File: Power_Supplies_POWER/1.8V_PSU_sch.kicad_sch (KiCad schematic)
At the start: 35 parts, among them IC6 TLV71209DBVT, IC7 TPS73618DBVTG4, IC8 TLV73333PDBVR, IC9 TLV73333PDBVR, J1 PINHD_1x4_Female, J23 PINHD_1x2_Female, J24 PINHD_1x2_Female, J25 Screw_Terminal_4_P5.00mm, J26 PINHD_1x1_Female, J28 PINHD_1x5_Female, J29 PINHD_1x2_Female, J30 PINHD_1x2_Female, J31 PINHD_1x2_Female, J32 PINHD_1x1_Female

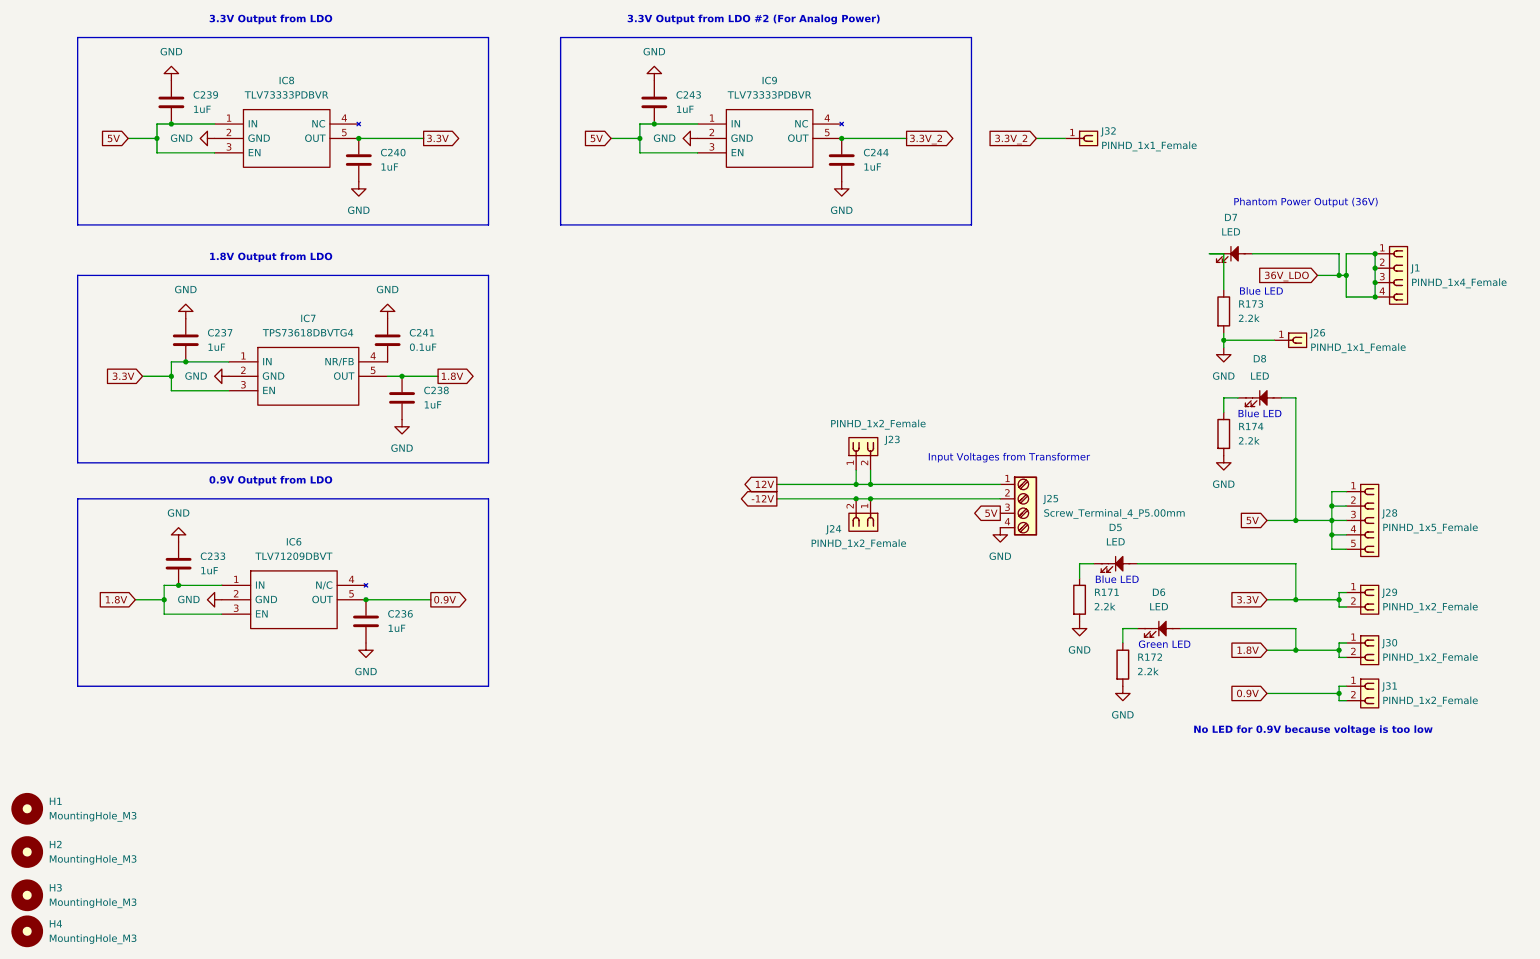
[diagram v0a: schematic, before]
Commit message: fixed power board problems/...
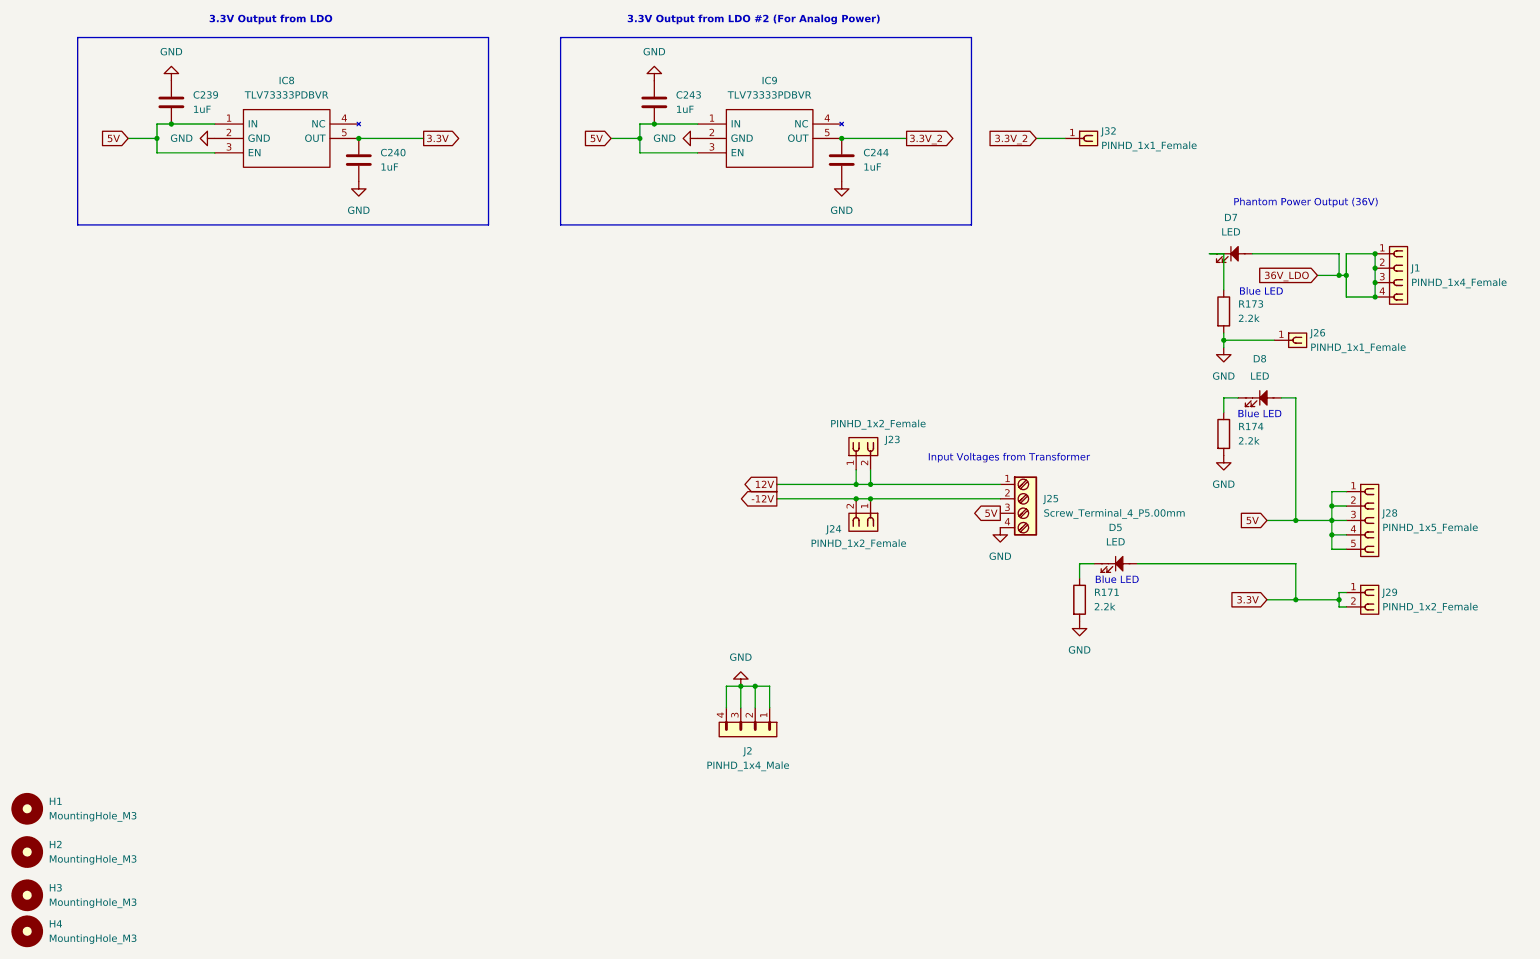
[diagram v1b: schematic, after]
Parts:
- removed C233, C236, C237, C238: 1uF, Capacitor_SMD:C_0402_1005Metric, symbol Device:C
- removed C241: 0.1uF, Capacitor_SMD:C_0402_1005Metric, symbol Device:C
- removed D6: LED, LED_SMD:LED_0402_1005Metric_Pad0.77x0.64mm_HandSolder, symbol PCM_SL_Devices:LED
- removed IC6: TLV71209DBVT, symbol SamacSys_Parts:TLV71209DBVT
- removed IC7: TPS73618DBVTG4, symbol SamacSys_Parts:TPS73618DBVTG4
- removed J30, J31: PINHD_1x2_Female, Connector_PinSocket_2.54mm:PinSocket_1x02_P2.54mm_Vertical, symbol PCM_SL_Pin_Headers:PINHD_1x2_Female
- removed R172: 2.2k, Resistor_SMD:R_0805_2012Metric, symbol Device:R
- added J2: PINHD_1x4_Male, Connector_PinHeader_2.54mm:PinHeader_1x04_P2.54mm_Vertical, symbol PCM_SL_Pin_Headers:PINHD_1x4_Male
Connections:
- net GND: now also J2.1, J2.2, J2.3, J2.4
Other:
- note removed: "0.9V Output from LDO"
- note removed: "1.8V Output from LDO"
- note removed: "Green LED"
- note removed: "No LED for 0.9V because voltage is too low"

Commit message: aaaah (cooked)
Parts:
- removed J26, J32: PINHD_1x1_Female, Connector_PinSocket_2.54mm:PinSocket_1x01_P2.54mm_Vertical, symbol PCM_SL_Pin_Headers:PINHD_1x1_Female
- added J26, J32: PINHD_1x2_Female, Connector_PinSocket_2.54mm:PinSocket_1x02_P2.54mm_Vertical, symbol PCM_SL_Pin_Headers:PINHD_1x2_Female
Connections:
- net 3.3V_2: now also J32.1, J32.2
- net GND: now also J26.1, J26.2
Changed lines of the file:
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@@
 	)
 	(junction
+		(at 238.76 73.66)
+		(diameter 0)
+		(color 0 0 0 0)
+	)
+	(junction
 		(at 250.19 119.38)
 		(diameter 0)
@@
 	)
 	(junction
+		(at 201.93 38.1)
+		(diameter 0)
+		(color 0 0 0 0)
+	)
+	(junction
 		(at 167.64 101.6)
 		(diameter 0)
@@
 	(wire
 		(pts
+			(xy 238.76 73.66) (xy 238.76 76.2)
+		)
+		(stroke
+			(width 0)
+			(type default)
+		)
+	)
+	(wire
+		(pts
 			(xy 248.92 105.41) (xy 248.92 102.87)
 		)
@@
 	(wire
 		(pts
+			(xy 201.93 38.1) (xy 201.93 40.64)
+		)
+		(stroke
+			(width 0)
+			(type default)
+		)
+	)
+	(wire
+		(pts
 			(xy 147.32 138.43) (xy 147.32 134.62)
 		)
@@
 	)
 	(symbol
-		(lib_id "PCM_SL_Pin_Headers:PINHD_1x1_Female")
-		(at 205.74 38.1 0)
-		(unit 1)
-		(exclude_from_sim no)
-		(in_bom yes)
-		(on_board yes)
-		(dnp no)
-		(fields_autoplaced yes)
-		(property "Reference" "J32"
-			(at 208.28 36.8299 0)
-			(effects
-				(font
-					(size 1.27 1.27)
-				)
-				(justify left)
-			)
-		)
-		(property "Value" "PINHD_1x1_Female"
-			(at 208.28 39.3699 0)
-			(effects
-				(font
-					(size 1.27 1.27)
-				)
-				(justify left)
-			)
-		)
-		(property "Footprint" "Connector_PinSocket_2.54mm:PinSocket_1x01_P2.54mm_Vertical"
-			(at 208.28 29.21 0)
-			(effects
-				(font
-					(size 1.27 1.27)
-				)
-				(hide yes)
-			)
-		)
-		(property "Datasheet" ""
-			(at 205.74 31.75 0)
-			(effects
-				(font
-					(size 1.27 1.27)
-				)
-				(hide yes)
-			)
-		)
-		(property "Description" "Pin Header female with pin space 2.54mm. Pin Count -1"
-			(at 205.74 38.1 0)
-			(effects
-				(font
-					(size 1.27 1.27)
-				)
-				(hide yes)
-			)
-		)
-		(pin "1"
-		)
-		(instances
-			(project "Power_Supplies_Copy"
-				(path "/5266cf9e-da90-4c53-80fd-cf3dbed42632/9c32f96f-6431-432f-ba4b-d32b848998a9"
-					(reference "J32")
-					(unit 1)
-				)
-			)
-		)
-	)
-	(symbol
 		(lib_id "PCM_SL_Pin_Headers:PINHD_1x4_Female")
 		(at 260.35 62.23 0)
@@
 	)
 	(symbol
-		(lib_id "PCM_SL_Pin_Headers:PINHD_1x1_Female")
-		(at 242.57 73.66 0)
-		(unit 1)
-		(exclude_from_sim no)
-		(in_bom yes)
-		(on_board yes)
-		(dnp no)
-		(fields_autoplaced yes)
-		(property "Reference" "J26"
-			(at 245.11 72.3899 0)
-			(effects
-				(font
-					(size 1.27 1.27)
-				)
-				(justify left)
-			)
-		)
-		(property "Value" "PINHD_1x1_Female"
-			(at 245.11 74.9299 0)
-			(effects
-				(font
-					(size 1.27 1.27)
-				)
-				(justify left)
-			)
-		)
-		(property "Footprint" "Connector_PinSocket_2.54mm:PinSocket_1x01_P2.54mm_Vertical"
-			(at 245.11 64.77 0)
-			(effects
-				(font
-					(size 1.27 1.27)
-				)
-				(hide yes)
-			)
-		)
-		(property "Datasheet" ""
-			(at 242.57 67.31 0)
-			(effects
-				(font
-					(size 1.27 1.27)
-				)
-				(hide yes)
-			)
-		)
-		(property "Description" "Pin Header female with pin space 2.54mm. Pin Count -1"
-			(at 242.57 73.66 0)
-			(effects
-				(font
-					(size 1.27 1.27)
-				)
-				(hide yes)
-			)
-		)
-		(pin "1"
-		)
-		(instances
-			(project "Power_Supplies_Copy"
-				(path "/5266cf9e-da90-4c53-80fd-cf3dbed42632/9c32f96f-6431-432f-ba4b-d32b848998a9"
-					(reference "J26")
-					(unit 1)
-				)
-			)
-		)
-	)
-	(symbol
 		(lib_id "power:GND")
 		(at 129.54 27.94 180)
@@
 	)
 	(symbol
+		(lib_id "PCM_SL_Pin_Headers:PINHD_1x2_Female")
+		(at 242.57 74.93 0)
+		(unit 1)
+		(exclude_from_sim no)
+		(in_bom yes)
+		(on_board yes)
+		(dnp no)
+		(fields_autoplaced yes)
+		(property "Reference" "J26"
+			(at 245.11 73.6599 0)
+			(effects
+				(font
+					(size 1.27 1.27)
+				)
+				(justify left)
+			)
+		)
+		(property "Value" "PINHD_1x2_Female"
+			(at 245.11 76.1999 0)
+			(effects
+				(font
+					(size 1.27 1.27)
+				)
+				(justify left)
+			)
+		)
+		(property "Footprint" "Connector_PinSocket_2.54mm:PinSocket_1x02_P2.54mm_Vertical"
+			(at 245.11 64.77 0)
+			(effects
+				(font
+					(size 1.27 1.27)
+				)
+				(hide yes)
+			)
+		)
+		(property "Datasheet" ""
+			(at 242.57 67.31 0)
+			(effects
+				(font
+					(size 1.27 1.27)
+				)
+				(hide yes)
+			)
+		)
+		(property "Description" "Pin Header female with pin space 2.54mm. Pin Count -2"
+			(at 242.57 74.93 0)
+			(effects
+				(font
+					(size 1.27 1.27)
+				)
+				(hide yes)
+			)
+		)
+		(pin "1"
+		)
+		(pin "2"
+		)
+		(instances
+			(project ""
+				(path "/5266cf9e-da90-4c53-80fd-cf3dbed42632/9c32f96f-6431-432f-ba4b-d32b848998a9"
+					(reference "J26")
+					(unit 1)
+				)
+			)
+		)
+	)
+	(symbol
 		(lib_id "PCM_SL_Pin_Headers:PINHD_1x5_Female")
 		(at 255.27 105.41 0)
@@
 					(unit 1)
 				)
+			)
+		)
+	)
+	(symbol
+		(lib_id "PCM_SL_Pin_Headers:PINHD_1x2_Female")
+		(at 205.74 39.37 0)
+		(unit 1)
+		(exclude_from_sim no)
+		(in_bom yes)
+		(on_board yes)
+		(dnp no)
+		(fields_autoplaced yes)
+		(property "Reference" "J32"
+			(at 208.28 38.0999 0)
+			(effects
+				(font
+					(size 1.27 1.27)
+				)
+				(justify left)
+			)
+		)
+		(property "Value" "PINHD_1x2_Female"
+			(at 208.28 40.6399 0)
+			(effects
+				(font
+					(size 1.27 1.27)
+				)
+				(justify left)
+			)
+		)
+		(property "Footprint" "Connector_PinSocket_2.54mm:PinSocket_1x02_P2.54mm_Vertical"
+			(at 208.28 29.21 0)
+			(effects
+				(font
+					(size 1.27 1.27)
+				)
+				(hide yes)
+			)
+		)
+		(property "Datasheet" ""
+			(at 205.74 31.75 0)
+			(effects
+				(font
+					(size 1.27 1.27)
+				)
+				(hide yes)
+			)
+		)
+		(property "Description" "Pin Header female with pin space 2.54mm. Pin Count -2"
+			(at 205.74 39.37 0)
+			(effects
+				(font
+					(size 1.27 1.27)
+				)
+				(hide yes)
+			)
+		)
+		(pin "2"
+		)
+		(pin "1"
+		)
+		(instances
+			(project ""
+				(path "/5266cf9e-da90-4c53-80fd-cf3dbed42632/9c32f96f-6431-432f-ba4b-d32b848998a9"
+					(reference "J32")
+					(unit 1)
+				)
